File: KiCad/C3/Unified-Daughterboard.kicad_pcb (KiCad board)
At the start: 2 copper layers, 18 x 16.5 mm, 14 parts, among them J1 TYPE-C-31-M12_13, J2 SM04B-SRSS-TB(LF)(SN), U1 TPD4E05U06DQAR

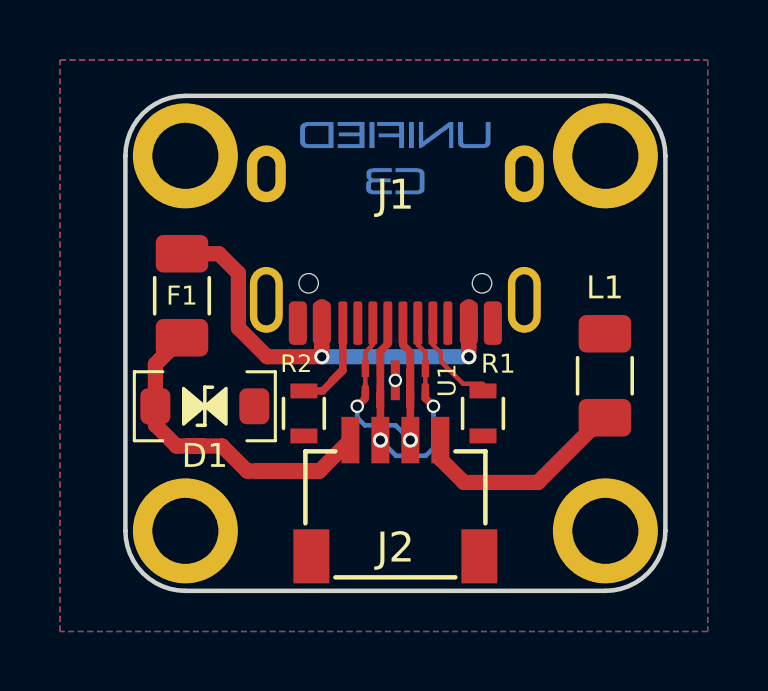
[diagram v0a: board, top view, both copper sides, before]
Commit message: fix submodule&missing footprint
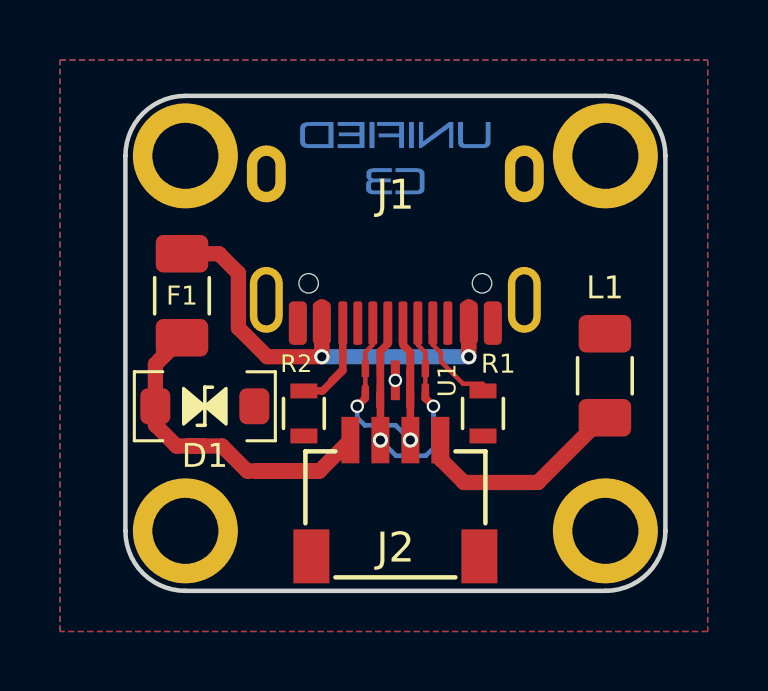
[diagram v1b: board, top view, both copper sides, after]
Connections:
- J1 pad A8: Net-(J1-PadA8) -> unconnected-(J1-PadA8)
- J1 pad B8: Net-(J1-PadB8) -> unconnected-(J1-PadB8)
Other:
- net class Default removed
- net class Power removed
